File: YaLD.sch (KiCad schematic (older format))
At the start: 17 parts, among them IC1 ATMEGA32-A, IC2 PCA9685, IC3 PCA9685, K1 IR_RCV, SW1 DIPS_10, U1 75LBC176, X1 16MHz

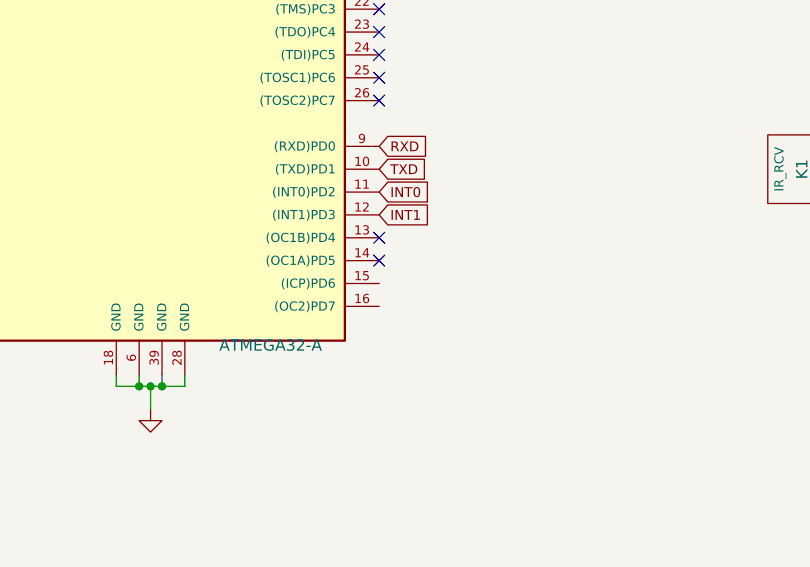
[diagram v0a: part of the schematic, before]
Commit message: fixed RJ45 connectors + folder libs.pretty added
RJ45 were on wrong side;
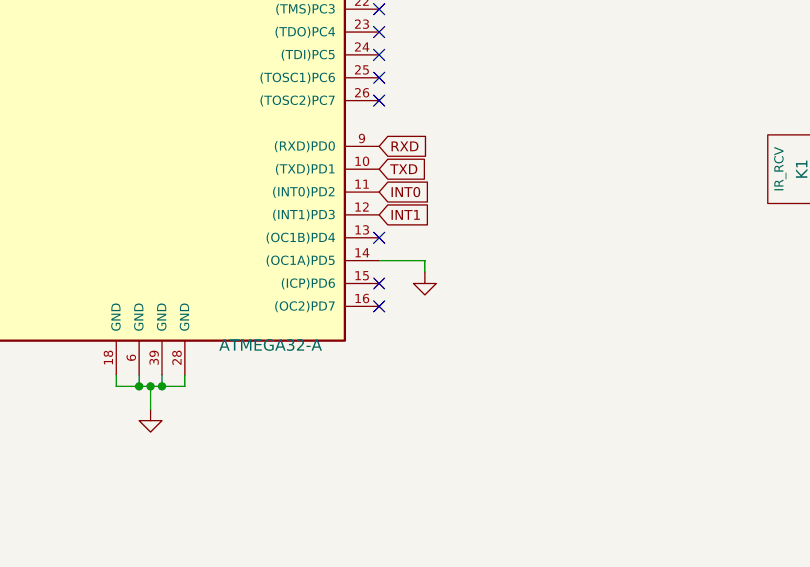
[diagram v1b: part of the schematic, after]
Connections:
- net GND: now also IC1.14 ((OC1A)PD5)
- no-connect marks 9 -> 10
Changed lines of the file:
@@
 NoConn ~ 4450 4150
 NoConn ~ 4450 4250
-NoConn ~ 4450 4850
-NoConn ~ 4450 4950
 NoConn ~ 2450 2950
 Wire Wire Line
@@
 Text GLabel 4450 2750 2    47   Input ~ 0
 DIP10
+NoConn ~ 4450 5050
+NoConn ~ 4450 5150
+NoConn ~ 4450 4850
+Wire Wire Line
+	4450 4950 4650 4950
+Wire Wire Line
+	4650 4950 4650 5000
+$Comp
+L GND #PWR021
+U 1 1 544EB0EF
+P 4650 5000
+F 0 "#PWR021" H 4650 5000 30  0001 C CNN
+F 1 "GND" H 4650 4930 30  0001 C CNN
+F 2 "" H 4650 5000 60  0000 C CNN
+F 3 "" H 4650 5000 60  0000 C CNN
+	1    4650 5000
+	1    0    0    -1
+$EndComp
 $EndSCHEMATC

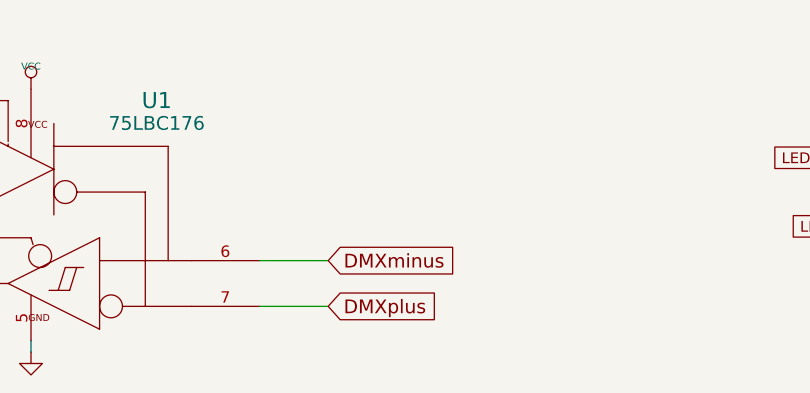
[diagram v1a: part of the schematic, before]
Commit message: DMX plus/minus switched, GND airwire connected
+ nicer silk print (more readable)
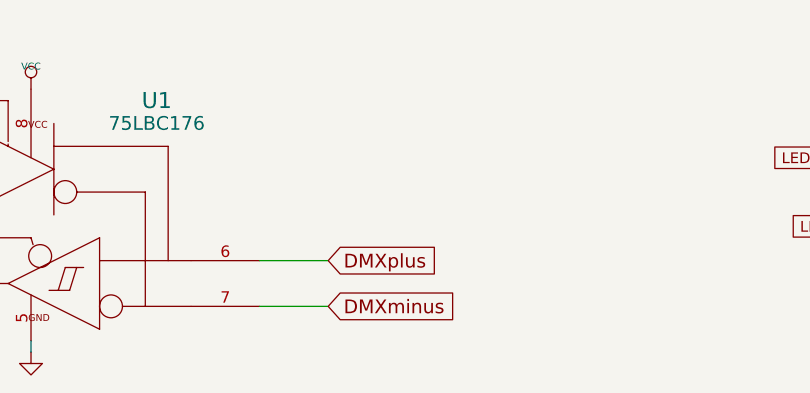
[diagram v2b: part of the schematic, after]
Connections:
- net DMXminus: now also U1.7 (BUS-); no longer U1.6 (BUS+)
- net DMXplus: now also U1.6 (BUS+); no longer U1.7 (BUS-)
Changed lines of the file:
@@
 $EndSheet
 Text GLabel 3050 7200 2    60   Input ~ 0
+DMXplus
+Text GLabel 3050 7400 2    60   Input ~ 0
 DMXminus
-Text GLabel 3050 7400 2    60   Input ~ 0
-DMXplus
 $Comp
 L PCA9685 IC2

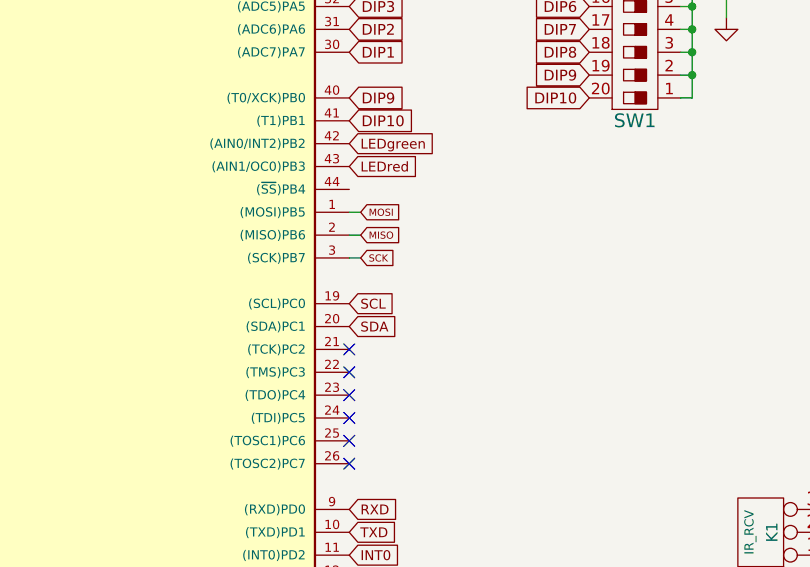
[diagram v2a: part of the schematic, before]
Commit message: added debug connector (software UART TX)
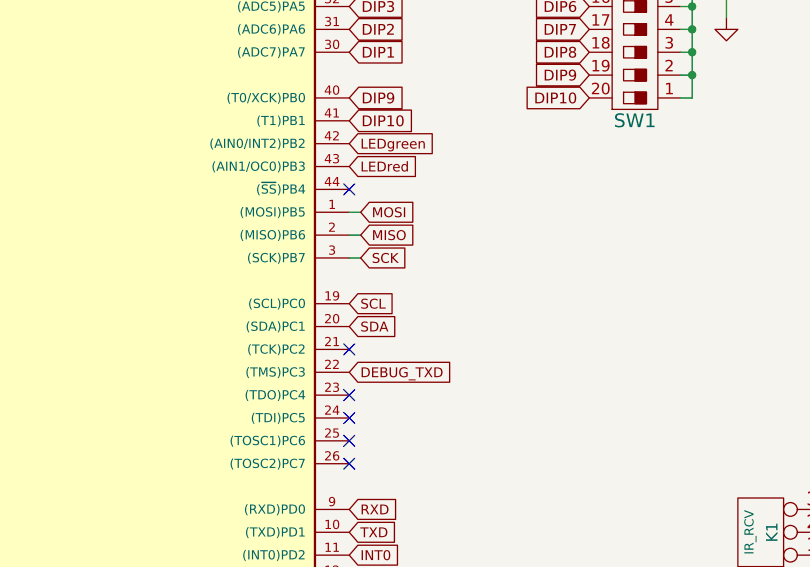
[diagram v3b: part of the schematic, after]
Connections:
- net DEBUG_TXD: now reaches IC1.22 ((TMS)PC3)
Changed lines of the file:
@@
 LIBS:contrib
 LIBS:valves
-LIBS:pca9685
-LIBS:dips-s
-LIBS:irf-2
-LIBS:conn_17x2
 LIBS:7805_f
 LIBS:YaLD-cache
@@
 	1    0    0    -1
 $EndComp
-Text GLabel 4500 3150 2    31   Input ~ 0
+Text GLabel 4500 3150 2    43   Input ~ 0
 MOSI
-Text GLabel 4500 3250 2    31   Input ~ 0
+Text GLabel 4500 3250 2    43   Input ~ 0
 MISO
-Text GLabel 4500 3350 2    31   Input ~ 0
+Text GLabel 4500 3350 2    43   Input ~ 0
 SCK
 Text GLabel 4450 4650 2    43   Input ~ 0
@@
 RESET
 NoConn ~ 4450 3750
-NoConn ~ 4450 3850
 NoConn ~ 4450 3950
 NoConn ~ 4450 4050
@@
 	1    0    0    -1
 $EndComp
+NoConn ~ 4450 3050
+Text GLabel 4450 3850 2    43   Input ~ 0
+DEBUG_TXD
 $EndSCHEMATC

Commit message: changed outputs to 3.5mm pitch
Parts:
- C1, C2: symbol C -> C-RESCUE-YaLD
- C3: symbol CP1 -> CP1-RESCUE-YaLD
- D1, D2: symbol LED -> LED-RESCUE-YaLD
- R1, R2, R3, R4, R5: symbol R -> R-RESCUE-YaLD
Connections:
- net INT1: now also K1.3 (P3); no longer K1.2 (PM)
- net at C3.1, R3.1: now also K1.2 (PM); no longer K1.3 (P3)
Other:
- moved on the sheet: C3
